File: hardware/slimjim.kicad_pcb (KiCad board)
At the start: 2 copper layers, 45.7 x 39.4 mm, 8 parts, among them J1 USB, P1 CONN_01X12, P2 CONN_01X12, SW1 RESET, U1 RF200, U2 TC200

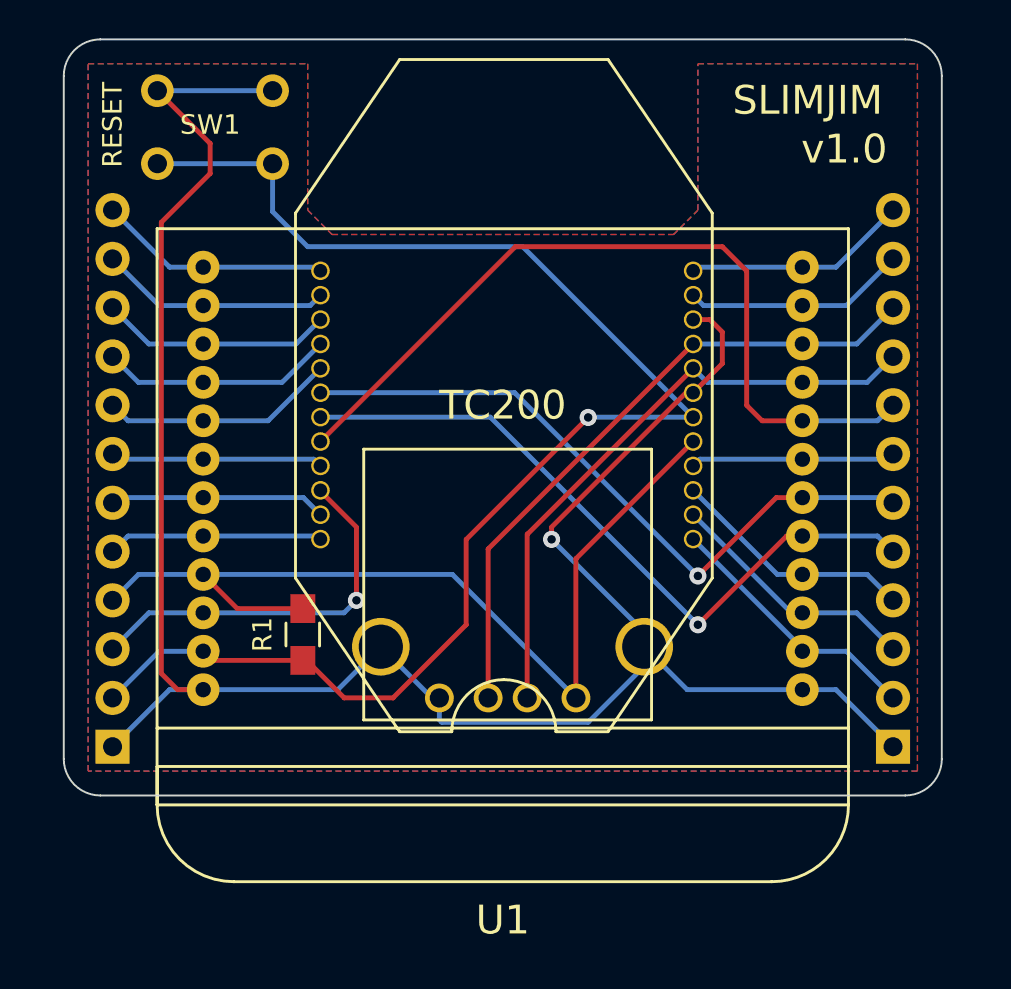
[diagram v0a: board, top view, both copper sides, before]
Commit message: Widen board and add pin silkscreens.
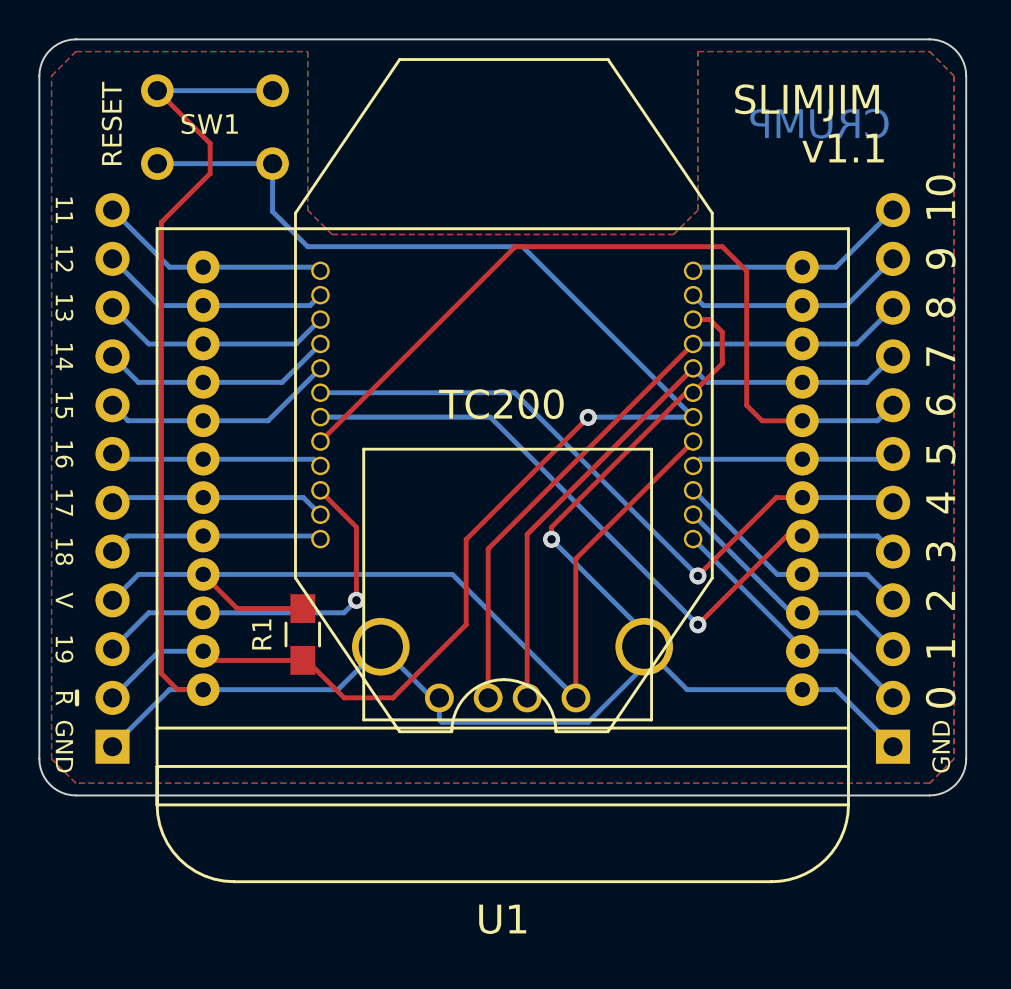
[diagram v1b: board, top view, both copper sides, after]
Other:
- board size 45.7 x 39.4 mm -> 48.3 x 39.4 mm
- board text added: "0"
- board text added: "1"
- board text added: "10"
- board text added: "11"
- board text added: "12"
- board text added: "13"
- board text added: "14"
- board text added: "15"
- board text added: "16"
- board text added: "17"
- board text added: "18"
- board text added: "19"
- board text added: "2"
- board text added: "3"
- board text added: "4"
- board text added: "5"
- board text added: "6"
- board text added: "7"
- board text added: "8"
- board text added: "9"
- board text added: "CRUMP"
- board text added: "GND"
- board text added: "V"
- board text added: "v1.1"
- board text added: "~R"
- board text removed: "v1.0"
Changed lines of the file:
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@@
-(kicad_pcb (version 4) (host pcbnew "(2014-12-04 BZR 5312)-product")
+(kicad_pcb (version 4) (host pcbnew 4.0.3-stable)
   (general
     (links 61)
     (no_connects 0)
-    (area 167.681001 76.261 223.479 125.979)
+    (area 168.859999 78.689999 217.220001 118.160001)
     (thickness 1.6)
-    (drawings 14)
+    (drawings 63)
     (tracks 155)
     (zones 0)
@@
       (xy 6.162389 -0.649564) (xy 6.186444 -1.510795) (xy 6.186444 -1.510795)) (layer B.SilkS) (width 0.1))
   )
-  (gr_text v1.0 (at 210.82 84.455) (layer F.SilkS)
+  (gr_text CRUMP (at 209.55 83.185) (layer B.Cu)
+    (effects (font (size 1.5 1.5) (thickness 0.3)) (justify mirror))
+  )
+  (gr_text ~R (at 170.1927 113.0427 270) (layer B.SilkS)
+    (effects (font (size 0.9 0.9) (thickness 0.225)) (justify mirror))
+  )
+  (gr_text GND (at 170.1927 115.5827 270) (layer B.SilkS)
+    (effects (font (size 0.9 0.9) (thickness 0.225)) (justify mirror))
+  )
+  (gr_text V (at 170.1927 107.9627 270) (layer B.SilkS)
+    (effects (font (size 0.9 0.9) (thickness 0.225)) (justify mirror))
+  )
+  (gr_text 19 (at 170.1927 110.5027 270) (layer B.SilkS)
+    (effects (font (size 0.9 0.9) (thickness 0.225)) (justify mirror))
+  )
+  (gr_text 14 (at 170.1927 95.2627 270) (layer B.SilkS)
+    (effects (font (size 0.9 0.9) (thickness 0.225)) (justify mirror))
+  )
+  (gr_text 13 (at 170.1927 92.7227 270) (layer B.SilkS)
+    (effects (font (size 0.9 0.9) (thickness 0.225)) (justify mirror))
+  )
+  (gr_text 11 (at 170.1927 87.6427 270) (layer B.SilkS)
+    (effects (font (size 0.9 0.9) (thickness 0.225)) (justify mirror))
+  )
+  (gr_text 12 (at 170.1927 90.1827 270) (layer B.SilkS)
+    (effects (font (size 0.9 0.9) (thickness 0.225)) (justify mirror))
+  )
+  (gr_text 16 (at 170.1927 100.3427 270) (layer B.SilkS)
+    (effects (font (size 0.9 0.9) (thickness 0.225)) (justify mirror))
+  )
+  (gr_text 15 (at 170.1927 97.8027 270) (layer B.SilkS)
+    (effects (font (size 0.9 0.9) (thickness 0.225)) (justify mirror))
+  )
+  (gr_text 17 (at 170.1927 102.8827 270) (layer B.SilkS)
+    (effects (font (size 0.9 0.9) (thickness 0.225)) (justify mirror))
+  )
+  (gr_text 18 (at 170.1927 105.4227 270) (layer B.SilkS)
+    (effects (font (size 0.9 0.9) (thickness 0.225)) (justify mirror))
+  )
+  (gr_text 18 (at 170.18 105.41 270) (layer F.SilkS)
+    (effects (font (size 0.9 0.9) (thickness 0.225)))
+  )
+  (gr_text 17 (at 170.18 102.87 270) (layer F.SilkS)
+    (effects (font (size 0.9 0.9) (thickness 0.225)))
+  )
+  (gr_text 15 (at 170.18 97.79 270) (layer F.SilkS)
+    (effects (font (size 0.9 0.9) (thickness 0.225)))
+  )
+  (gr_text 16 (at 170.18 100.33 270) (layer F.SilkS)
+    (effects (font (size 0.9 0.9) (thickness 0.225)))
+  )
+  (gr_text 12 (at 170.18 90.17 270) (layer F.SilkS)
+    (effects (font (size 0.9 0.9) (thickness 0.225)))
+  )
+  (gr_text 11 (at 170.18 87.63 270) (layer F.SilkS)
+    (effects (font (size 0.9 0.9) (thickness 0.225)))
+  )
+  (gr_text 13 (at 170.18 92.71 270) (layer F.SilkS)
+    (effects (font (size 0.9 0.9) (thickness 0.225)))
+  )
+  (gr_text 14 (at 170.18 95.25 270) (layer F.SilkS)
+    (effects (font (size 0.9 0.9) (thickness 0.225)))
+  )
+  (gr_text 19 (at 170.18 110.49 270) (layer F.SilkS)
+    (effects (font (size 0.9 0.9) (thickness 0.225)))
+  )
+  (gr_text V (at 170.18 107.95 270) (layer F.SilkS)
+    (effects (font (size 0.9 0.9) (thickness 0.225)))
+  )
+  (gr_text GND (at 170.18 115.57 270) (layer F.SilkS)
+    (effects (font (size 0.9 0.9) (thickness 0.225)))
+  )
+  (gr_text ~R (at 170.18 113.03 270) (layer F.SilkS)
+    (effects (font (size 0.9 0.9) (thickness 0.225)))
+  )
+  (gr_text 1 (at 215.9 110.49 90) (layer B.SilkS)
+    (effects (font (size 1.5 1.5) (thickness 0.3)) (justify mirror))
+  )
+  (gr_text 2 (at 215.9 107.95 90) (layer B.SilkS)
+    (effects (font (size 1.5 1.5) (thickness 0.3)) (justify mirror))
+  )
+  (gr_text 3 (at 215.9 105.41 90) (layer B.SilkS)
+    (effects (font (size 1.5 1.5) (thickness 0.3)) (justify mirror))
+  )
+  (gr_text 4 (at 215.9 102.87 90) (layer B.SilkS)
+    (effects (font (size 1.5 1.5) (thickness 0.3)) (justify mirror))
+  )
+  (gr_text 5 (at 215.9 100.33 90) (layer B.SilkS)
+    (effects (font (size 1.5 1.5) (thickness 0.3)) (justify mirror))
+  )
+  (gr_text 6 (at 215.9 97.79 90) (layer B.SilkS)
+    (effects (font (size 1.5 1.5) (thickness 0.3)) (justify mirror))
+  )
+  (gr_text 7 (at 215.9 95.25 90) (layer B.SilkS)
+    (effects (font (size 1.5 1.5) (thickness 0.3)) (justify mirror))
+  )
+  (gr_text 8 (at 215.9 92.71 90) (layer B.SilkS)
+    (effects (font (size 1.5 1.5) (thickness 0.3)) (justify mirror))
+  )
+  (gr_text 9 (at 215.9 90.17 90) (layer B.SilkS)
+    (effects (font (size 1.5 1.5) (thickness 0.3)) (justify mirror))
+  )
+  (gr_text "0\n" (at 215.9 113.03 90) (layer B.SilkS)
+    (effects (font (size 1.5 1.5) (thickness 0.3)) (justify mirror))
+  )
+  (gr_text GND (at 215.9 115.57 90) (layer B.SilkS)
+    (effects (font (size 0.9 0.9) (thickness 0.225)) (justify mirror))
+  )
+  (gr_text 10 (at 215.9 86.995 90) (layer B.SilkS)
+    (effects (font (size 1.5 1.5) (thickness 0.3)) (justify mirror))
+  )
+  (gr_text 10 (at 215.9 86.995 90) (layer F.SilkS)
+    (effects (font (size 1.5 1.5) (thickness 0.3)))
+  )
+  (gr_text GND (at 215.9 115.57 90) (layer F.SilkS)
+    (effects (font (size 0.9 0.9) (thickness 0.225)))
+  )
+  (gr_text "0\n" (at 215.9 113.03 90) (layer F.SilkS)
+    (effects (font (size 1.5 1.5) (thickness 0.3)))
+  )
+  (gr_text 9 (at 215.9 90.17 90) (layer F.SilkS)
+    (effects (font (size 1.5 1.5) (thickness 0.3)))
+  )
+  (gr_text 8 (at 215.9 92.71 90) (layer F.SilkS)
+    (effects (font (size 1.5 1.5) (thickness 0.3)))
+  )
+  (gr_text 7 (at 215.9 95.25 90) (layer F.SilkS)
+    (effects (font (size 1.5 1.5) (thickness 0.3)))
+  )
+  (gr_text 6 (at 215.9 97.79 90) (layer F.SilkS)
+    (effects (font (size 1.5 1.5) (thickness 0.3)))
+  )
+  (gr_text 5 (at 215.9 100.33 90) (layer F.SilkS)
+    (effects (font (size 1.5 1.5) (thickness 0.3)))
+  )
+  (gr_text 4 (at 215.9 102.87 90) (layer F.SilkS)
+    (effects (font (size 1.5 1.5) (thickness 0.3)))
+  )
+  (gr_text 3 (at 215.9 105.41 90) (layer F.SilkS)
+    (effects (font (size 1.5 1.5) (thickness 0.3)))
+  )
+  (gr_text 2 (at 215.9 107.95 90) (layer F.SilkS)
+    (effects (font (size 1.5 1.5) (thickness 0.3)))
+  )
+  (gr_text 1 (at 215.9 110.49 90) (layer F.SilkS)
+    (effects (font (size 1.5 1.5) (thickness 0.3)))
+  )
+  (gr_line (start 170.815 118.11) (end 215.265 118.11) (angle 90) (layer Edge.Cuts) (width 0.1))
+  (gr_line (start 215.265 78.74) (end 170.815 78.74) (angle 90) (layer Edge.Cuts) (width 0.1))
+  (gr_text v1.1 (at 210.82 84.455) (layer F.SilkS)
     (effects (font (size 1.5 1.5) (thickness 0.3)))
   )
@@
     (effects (font (size 1.5 1.5) (thickness 0.3)) (justify mirror))
   )
-  (gr_line (start 172.085 78.74) (end 213.995 78.74) (angle 90) (layer Edge.Cuts) (width 0.1))
-  (gr_line (start 170.18 116.205) (end 170.18 80.645) (angle 90) (layer Edge.Cuts) (width 0.1))
-  (gr_line (start 213.995 118.11) (end 172.085 118.11) (angle 90) (layer Edge.Cuts) (width 0.1))
-  (gr_line (start 215.9 80.645) (end 215.9 116.205) (angle 90) (layer Edge.Cuts) (width 0.1))
-  (gr_arc (start 213.995 116.205) (end 215.9 116.205) (angle 90) (layer Edge.Cuts) (width 0.1))
-  (gr_arc (start 172.085 116.205) (end 172.085 118.11) (angle 90) (layer Edge.Cuts) (width 0.1))
-  (gr_arc (start 172.085 80.645) (end 170.18 80.645) (angle 90) (layer Edge.Cuts) (width 0.1))
-  (gr_arc (start 213.995 80.645) (end 213.995 78.74) (angle 90) (layer Edge.Cuts) (width 0.1))
+  (gr_line (start 168.91 116.205) (end 168.91 80.645) (angle 90) (layer Edge.Cuts) (width 0.1))
+  (gr_line (start 217.17 80.645) (end 217.17 116.205) (angle 90) (layer Edge.Cuts) (width 0.1))
+  (gr_arc (start 215.265 116.205) (end 217.17 116.205) (angle 90) (layer Edge.Cuts) (width 0.1))
+  (gr_arc (start 170.815 116.205) (end 170.815 118.11) (angle 90) (layer Edge.Cuts) (width 0.1))
+  (gr_arc (start 170.815 80.645) (end 168.91 80.645) (angle 90) (layer Edge.Cuts) (width 0.1))
+  (gr_arc (start 215.265 80.645) (end 215.265 78.74) (angle 90) (layer Edge.Cuts) (width 0.1))
   (segment (start 210.39 112.6) (end 213.36 115.57) (width 0.254) (layer B.Cu) (net 1))
   (segment (start 208.64 112.6) (end 210.39 112.6) (width 0.254) (layer B.Cu) (net 1))
@@
     (polygon
       (pts
-        (xy 214.63 116.84) (xy 171.45 116.84) (xy 171.45 80.01) (xy 182.88 80.01) (xy 182.88 87.63)
-        (xy 184.15 88.9) (xy 201.93 88.9) (xy 203.2 87.63) (xy 203.2 80.01) (xy 214.63 80.01)
+        (xy 215.265 117.475) (xy 170.815 117.475) (xy 169.545 116.205) (xy 169.545 80.645) (xy 170.815 79.375)
+        (xy 182.88 79.375) (xy 182.88 87.63) (xy 184.15 88.9) (xy 201.93 88.9) (xy 203.2 87.63)
+        (xy 203.2 79.375) (xy 215.265 79.375) (xy 216.535 80.645) (xy 216.535 116.205)
       )
     )
@@
     (polygon
       (pts
-        (xy 214.63 116.84) (xy 171.45 116.84) (xy 171.45 80.01) (xy 182.88 80.01) (xy 182.88 87.63)
-        (xy 184.15 88.9) (xy 201.93 88.9) (xy 203.2 87.63) (xy 203.2 80.01) (xy 214.63 80.01)
+        (xy 215.265 117.475) (xy 170.815 117.475) (xy 169.545 116.205) (xy 169.545 80.645) (xy 170.815 79.375)
+        (xy 182.88 79.375) (xy 182.88 87.63) (xy 184.15 88.9) (xy 201.93 88.9) (xy 203.2 87.63)
+        (xy 203.2 79.375) (xy 215.265 79.375) (xy 216.535 80.645) (xy 216.535 116.205)
       )
     )

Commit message: Clean up silkscreens for RF200 and TC200.
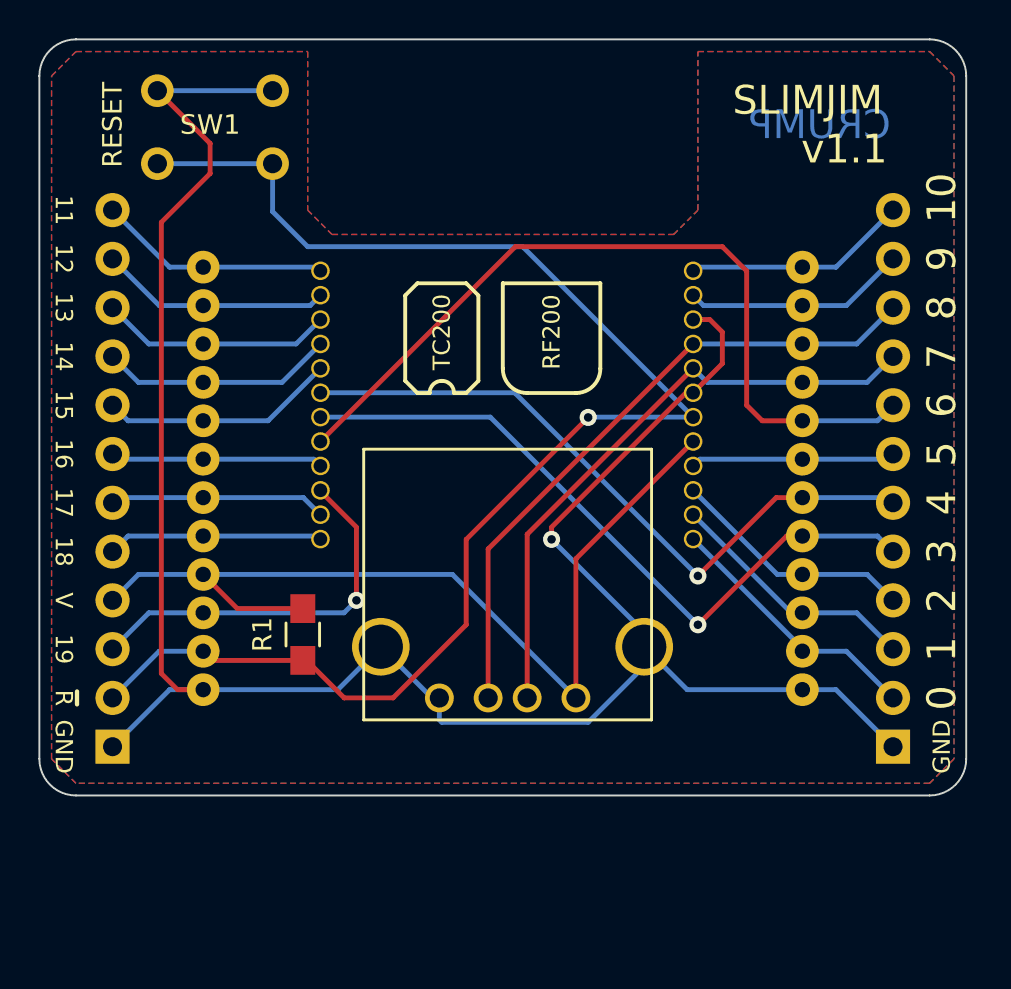
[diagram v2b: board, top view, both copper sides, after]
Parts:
- U1: footprint _CrumpPrints:RF200 -> _CrumpPrints:RF200_nosilk
- U2: footprint _CrumpPrints:TC200 -> _CrumpPrints:TC200_nosilk
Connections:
- net RF_24 renamed RF_1
- net TC_1 renamed RF_13
- net TC_11 renamed RF_19
- net TC_12 renamed RF_20
- net TC_17 renamed RF_21
- net TC_21 renamed RF_10
- net TC_23 renamed RF_11
- net TC_3 renamed RF_15
- net TC_5 renamed RF_17
- net TC_6 renamed RF_6
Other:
- board text added: "RF200"
- board text added: "TC200"
